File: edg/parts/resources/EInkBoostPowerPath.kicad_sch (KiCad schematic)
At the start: 10 parts

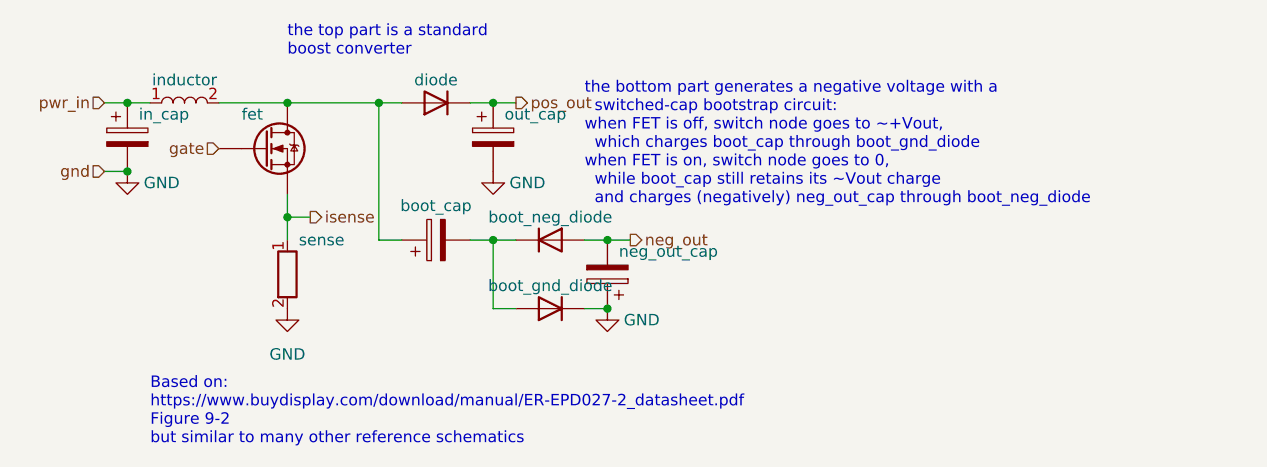
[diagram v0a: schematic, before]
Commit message: Nondirectioned Ground refactor (#364)
This introduces a dedicated non-directioned Ground type, with an
optional GroundReference which can specify the voltage level. Ground can
optionally specify a voltage tolerance.

Prior, Ground was actually just a VoltageSink in disguise, which had a
few problems stemming from the VoltageSink/VoltageSource directionality
that this fixes:
- Avoids needing explicit VoltageSource merges when connecting the
ground of multiple power supplies, eg USB + battery
- Avoids a confusing gnd and gnd_src for devices that can source or sink
power
- Eliminates unused current_draw parameter

This refactors a lot of internal libraries. Notable structural changes:
- BLDC driver current-sense resistors moved into the block, generating
if the sense pins are used.
- Ditto with the soldering iron connector
- Gate driver switch node is now a Ground
- Unify gnd and gnd_src for blocks that have both
- DecouplingCapacitor defined in terms of gnd/voltage instead of pos/neg

This change is breaking and requires some changes to top-level designs:
- Voltage-source merges for grounds for multiple power sources must be
removed
- GroundSource should be replaced with Ground (remapped with a
deprecation)
- VoltageTestPoint must be replaced with GroundTestPoint, now that the
types are different
- In general, ground-side current sense resistors are more difficult
now, the move so far is to move them into the associated block

Library cleanup to support offset grounds is needed in the future, to
make sure all devices use VoltageSink.from_gnd to use a ground-relative
voltage instead of assuming ground is 0v.

Also some internal cleanup.

Notes for the future:
- Some things that might need further thought
- Is there a clean unified way to get the voltage of a port accounting
for connected-ness and directionality? Currently, we have
`GroundLink._voltage_range` and `VoltageLink,_voltage_range`, though
code that doesn't need to be 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
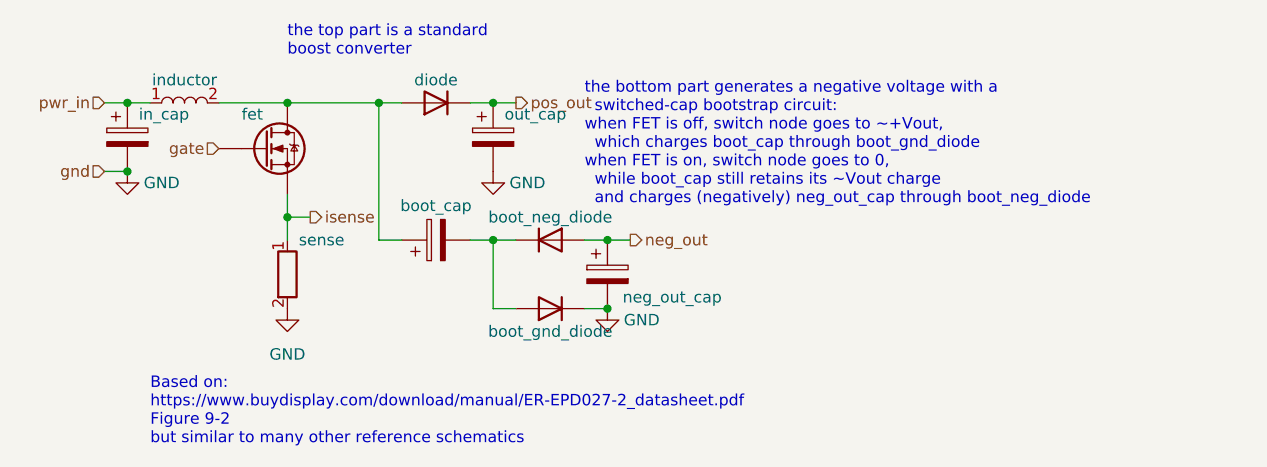
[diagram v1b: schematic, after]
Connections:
- net GND: now also neg_out_cap.2; no longer neg_out_cap.1
- net neg_out: now also neg_out_cap.1; no longer neg_out_cap.2
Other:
- moved on the sheet: neg_out_cap
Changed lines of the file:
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@@
     )
   )
-  (symbol (lib_id "Device:C_Polarized") (at 167.64 95.25 180) (unit 1)
+  (symbol (lib_id "Device:C_Polarized") (at 167.64 95.25 0) (unit 1)
     (in_bom yes) (on_board yes) (dnp no)
-    (property "Reference" "neg_out_cap" (at 168.91 92.71 0)
+    (property "Reference" "neg_out_cap" (at 180.34 97.79 0)
       (effects (font (size 1.27 1.27)) (justify right))
     )
-    (property "Value" "~" (at 171.45 97.4089 0)
+    (property "Value" "~" (at 163.83 93.0911 0)
       (effects (font (size 1.27 1.27)) (justify right))
     )
-    (property "Footprint" "" (at 166.6748 91.44 0)
+    (property "Footprint" "" (at 168.6052 99.06 0)
       (effects (font (size 1.27 1.27)) hide)
     )
@@
   (symbol (lib_id "Device:D") (at 161.29 99.06 180) (unit 1)
     (in_bom yes) (on_board yes) (dnp no)
-    (property "Reference" "boot_gnd_diode" (at 161.29 96.52 0)
+    (property "Reference" "boot_gnd_diode" (at 161.29 101.6 0)
       (effects (font (size 1.27 1.27)))
     )
